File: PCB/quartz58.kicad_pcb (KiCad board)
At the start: 2 copper layers, 334.4 x 146 mm, 198 parts, among them J1 OLED_128x32, J2 OLED_128x32, J3 Conn_01x10_Socket, J4 Conn_01x10_Pin, SW1 SW_SPDT, SW2 SW_Push, SW3 SW_SPDT, SW4 SW_Push, T1 TPS65-201A-S, U1 Nice_Nano_V2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

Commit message: updates
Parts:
- BT1, BT2: footprint ScottoKeebs_Components:Connector_1x02_JST-PH -> Connector_JST:JST_PH_S2B-PH-K_1x02_P2.00mm_Horizontal; moved to F.Cu
- moved BT1 3.10 mm to (170.3, 84.3), turned to 0 degrees
- moved BT2 3.00 mm to (256.0, 84.3), turned to 0 degrees
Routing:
- net GND: track 1799.3 -> 1806.8 mm
- net L-BATTERY-POSITIVE: track 54.3 -> 56.3 mm
- net R-BATTERY-POSITIVE: track 54.7 -> 53.1 mm
- net +3V3: track 1482.6 -> 1481.3 mm
- net Net-(SW1-B): track 63.1 -> 64.0 mm
- net L-RST: track 63.5 -> 64.2 mm
- net R-NRST: track 69.6 -> 69.1 mm

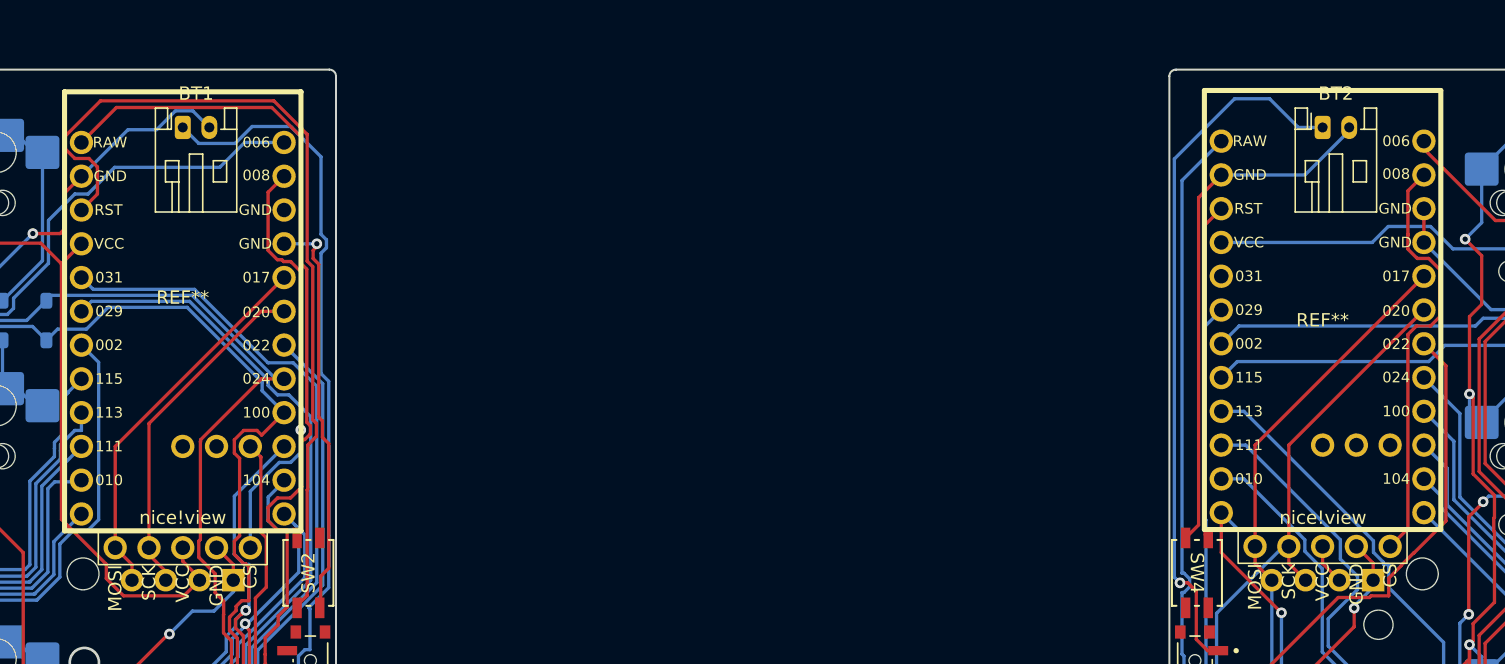
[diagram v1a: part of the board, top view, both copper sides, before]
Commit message: updates to jst connector
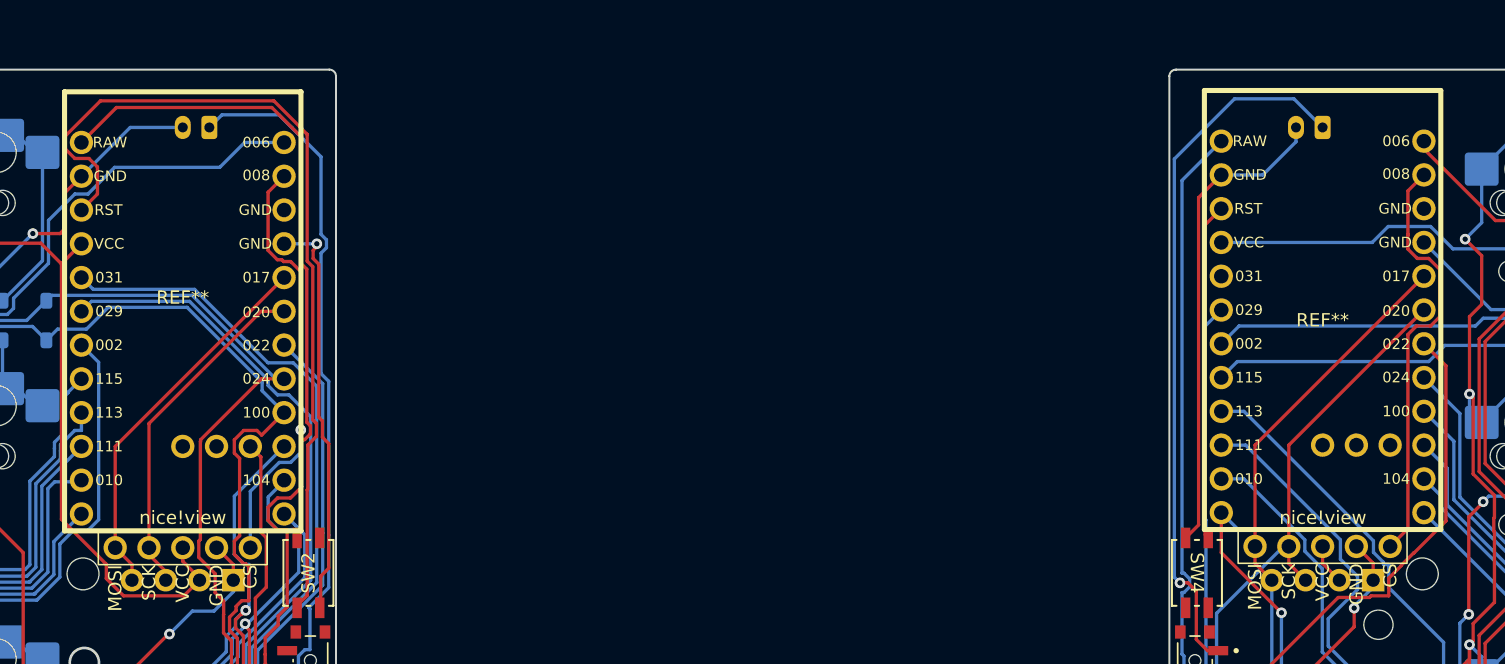
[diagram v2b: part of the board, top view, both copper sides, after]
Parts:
- BT1, BT2: moved to B.Cu
- moved BT1 2.00 mm to (172.3, 84.3), turned to 180 degrees
- turned BT2 to 180 degrees
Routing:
- net GND: track 1806.8 -> 1797.5 mm
- net L-BATTERY-POSITIVE: track 56.3 -> 54.1 mm
